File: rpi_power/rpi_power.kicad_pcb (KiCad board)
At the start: 2 copper layers, 99 x 99 mm, 131 parts, among them J1 POWER, J10 POWER, J2 Raspberry_Pi_2_3, J3 SENSORS, J4 ADCs, J5 DB25_Female, J6 SWITCHES, J7 PROG, J8 DB15_Female_MountingHoles, J9 GPIO, Q1 IRLML6344TRPBF, Q10 IRLML6344TRPBF, Q11 IRLML6344TRPBF, Q2 IRLML6344TRPBF, Q3 IRLML6344TRPBF, Q4 IRLML6344TRPBF, Q5 IRLML6344TRPBF, Q6 IRLML6344TRPBF, Q7 NPN, Q8 IRLML6344TRPBF, Q9 IRLML6344TRPBF, U1 TPS54625, U2 ATxmega16A4U-AU, U3 LM2936-3.3, Y1 Crystal

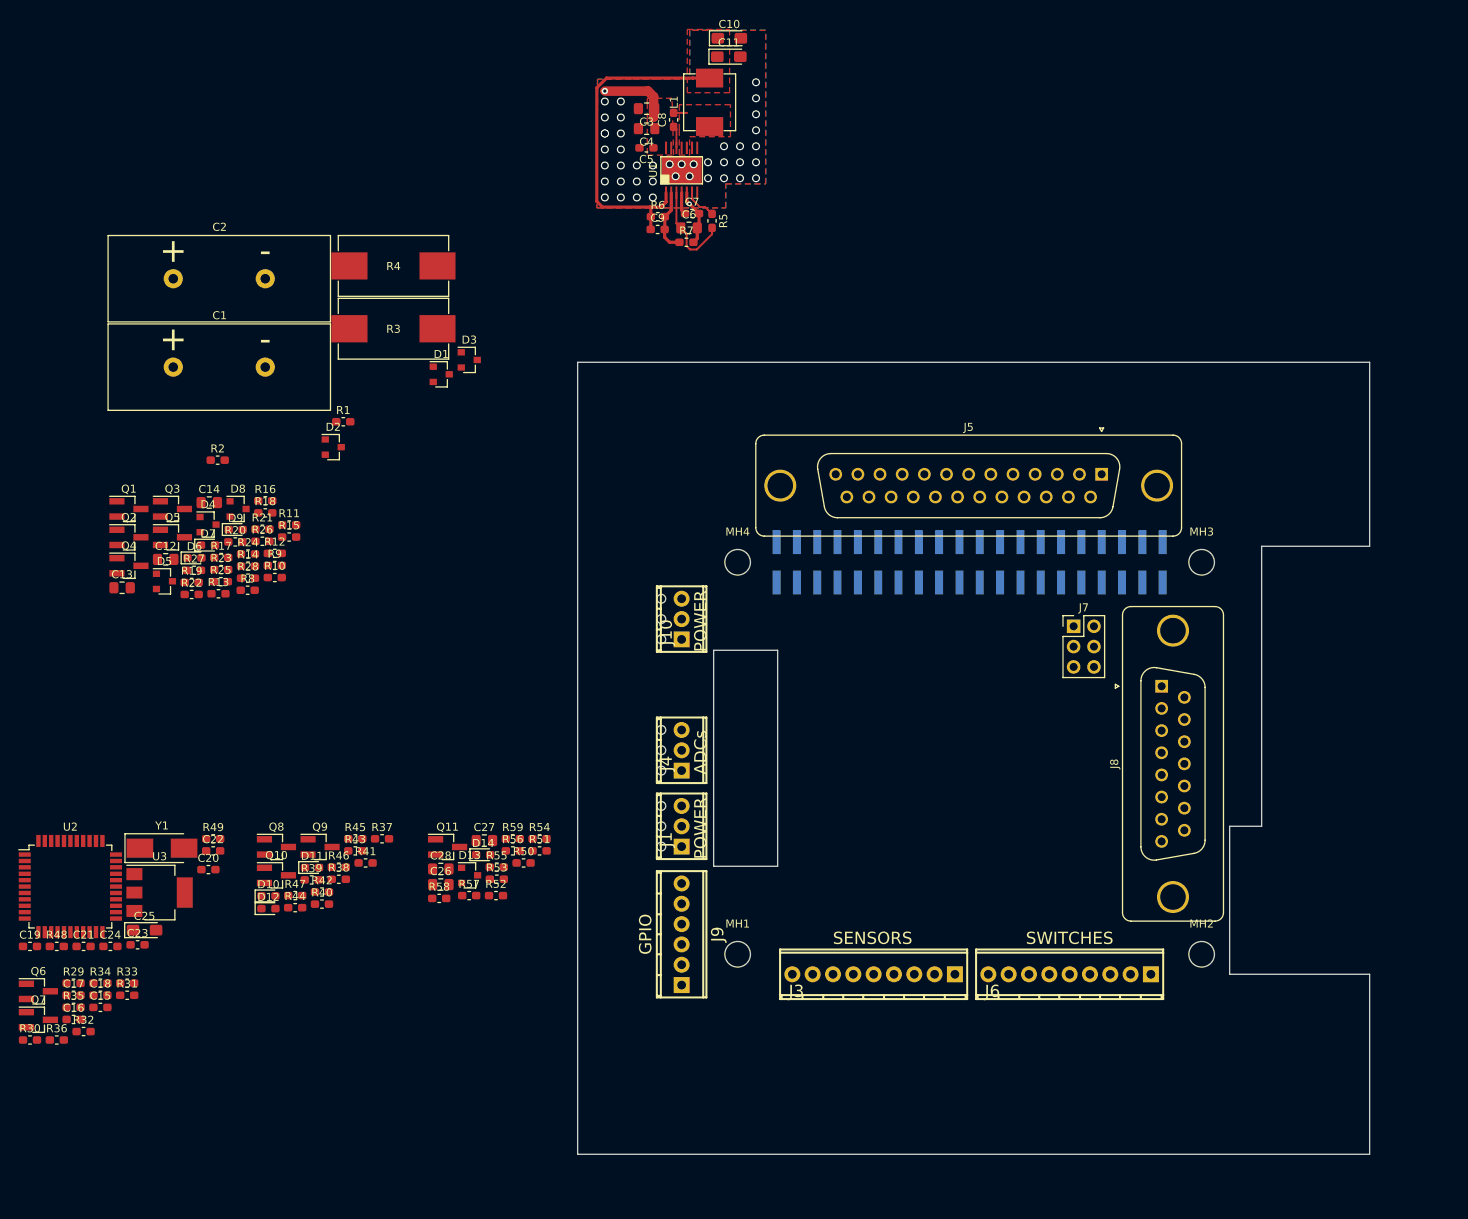
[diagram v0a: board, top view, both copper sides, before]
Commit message: Branched from cellar_board repo. Cleaned up unnecessary items.
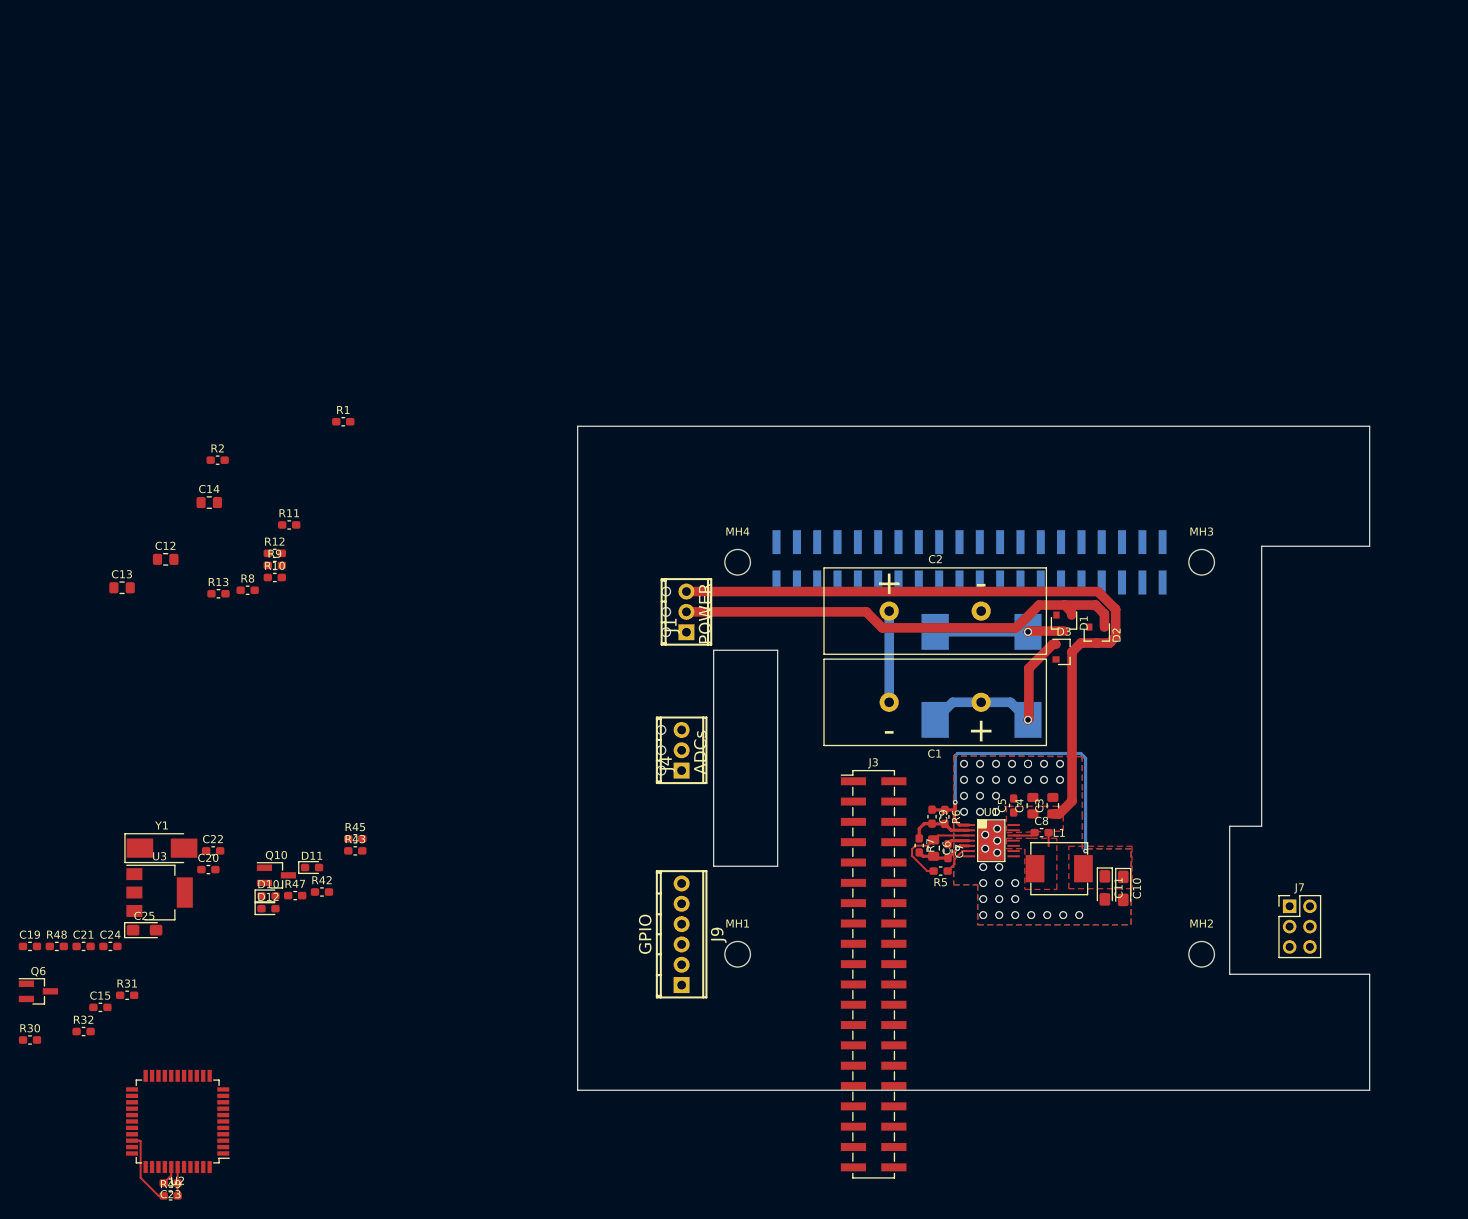
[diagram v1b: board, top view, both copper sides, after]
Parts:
- removed C16, C17, C18: 0.1uF/50V, Capacitor_SMD:C_0603_1608Metric_Pad1.05x0.95mm_HandSolder
- removed C26, C27, C28: UNKN, Capacitor_SMD:C_0805_2012Metric_Pad1.15x1.40mm_HandSolder
- removed D13, D4, D5, D8: SBR160S23-7, Diode_SMD:D_SOT-23_ANK
- removed D14, D6, D7, D9: LED_GREEN, LED_SMD:LED_0603_1608Metric_Pad1.05x0.95mm_HandSolder
- removed J10: POWER, w_conn_mpt:mpt_0,5-3-2,54
- removed J5: DB25_Female, Connectors_custom:DSUB-25_Female_Vertical_P2.77x2.84mm_MountingHoles
- removed J6: SWITCHES, w_conn_mpt:mpt_0,5-9-2,54
- removed J8: DB15_Female_MountingHoles, Connectors_custom:DSUB-15_Female_Vertical_P2.77x2.84mm_MountingHoles
- removed Q1, Q11, Q2, Q3, Q4, Q5, Q8, Q9: IRLML6344TRPBF, Package_TO_SOT_SMD:SOT-23_Handsoldering
- removed Q7: NPN, Package_TO_SOT_SMD:SOT-23_Handsoldering
- removed R14, R16, R17, R23, R26, R35, R37, R38, R41, R52: 10k, Resistor_SMD:R_0603_1608Metric_Pad1.05x0.95mm_HandSolder
- removed R15, R24, R25, R50, R51: 0, Resistor_SMD:R_0603_1608Metric_Pad1.05x0.95mm_HandSolder
- removed R18, R19, R27, R44, R46: 255, Resistor_SMD:R_0603_1608Metric_Pad1.05x0.95mm_HandSolder
- removed R20, R21, R28, R53: 1k, Resistor_SMD:R_0603_1608Metric_Pad1.05x0.95mm_HandSolder
- removed R22, R29, R33: 4.7k, Resistor_SMD:R_0603_1608Metric_Pad1.05x0.95mm_HandSolder
- removed R34, R40: 51k, Resistor_SMD:R_0603_1608Metric_Pad1.05x0.95mm_HandSolder
- removed R36, R39: 100k, Resistor_SMD:R_0603_1608Metric_Pad1.05x0.95mm_HandSolder
- removed R54, R55, R56, R57, R58, R59: UNKN, Resistor_SMD:R_0603_1608Metric_Pad1.05x0.95mm_HandSolder
- C12, C13, C14: value 10uF/25V -> UNKN
- J3: value SENSORS -> Raspberry_Pi_2_3; footprint w_conn_mpt:mpt_0,5-9-2,54 -> Connector_PinHeader_2.54mm:PinHeader_2x20_P2.54mm_Vertical_SMD
- R10: value 10k -> UNKN
- R11, R12, R13: value 0 -> UNKN
- R3, R4: moved to B.Cu
- R8, R9: value 4.7k -> UNKN
- moved C10 117.1 mm to (168.2, 111.8), turned to 270 degrees
- moved C11 114.0 mm to (165.9, 111.7), turned to 270 degrees
- moved L1 105.3 mm to (160.2, 109.3), turned to 0 degrees
- moved C3 100.8 mm to (159.4, 101.4), turned to 90 degrees
- moved C8 100.3 mm to (158.0, 104.8), turned to 0 degrees
- moved C1 98.8 mm to (144.7, 88.5), turned to 180 degrees
- moved C2 98.7 mm to (144.7, 77.1)
- moved D2 98.3 mm to (164.9, 80.1), turned to 270 degrees
- moved C4 97.4 mm to (156.9, 101.4), turned to 90 degrees
- moved C5 94.1 mm to (154.5, 101.4), turned to 90 degrees
- moved U1 92.3 mm to (151.7, 105.8), turned to 0 degrees
- moved R3 90.4 mm to (156.3, 85.2), turned to 90 degrees
- moved R5 86.2 mm to (145.4, 109.6), turned to 180 degrees
- moved C7 85.9 mm to (146.3, 107.1), turned to 270 degrees
- moved R4 84.9 mm to (144.7, 85.2), turned to 90 degrees
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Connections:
- C12 pad 1: HEAT_LEVER_F -> ADC1
- C13 pad 1: FAN_LEVER_F -> ADC2
- C14 pad 1: DEHUM_LEVER_F -> ADC3
- J2 pad 10: UART_RX_3V3 -> 10
- J2 pad 11: DHT22_EXT -> 11
- J2 pad 12: SERVO_PWM -> 12
- J2 pad 13: SERVO_ON-OFF -> 13
- J2 pad 16: FAN_LEVER_F -> 16
- J2 pad 18: LIGHT_SENSOR -> 18
- J2 pad 19: SPI0_MOSI -> 19
- J2 pad 21: SPI0_MISO -> 21
- J2 pad 22: HEAT_SWITCH -> 22
- J2 pad 23: SPI0_SCLK -> 23
- J2 pad 24: SPI0_CE -> 24
- J2 pad 26: SPI1_CE -> 26
- J2 pad 27: RESET_LEVER -> 27
- J2 pad 28: SWITCH0 -> 28
- J2 pad 29: HEAT_LEVER_F -> 29
- J2 pad 31: DEHUM_SWITCH -> 31
- J2 pad 32: DEHUM_LEVER_F -> 32
- J2 pad 33: FAN_SWITCH -> 33
- J2 pad 35: SPI1_MISO -> 35
- J2 pad 38: SPI1_MOSI -> 38
- J2 pad 40: SPI1_SCLK -> 40
- J2 pad 7: DHT22_INT -> 7
- J2 pad 8: UART_TX_3V3 -> 8
- J3 pad 1: GND -> +3V3
- J3 pad 2: +3V3 -> +5V
- J3 pad 3: DHT22_INT -> I2C_SDA
- J3 pad 4: GND -> +5V
- J3 pad 5: +3V3 -> I2C_SCL
- J3 pad 6: DHT22_EXT -> GND
- J3 pad 7: +3V3 -> 7
- J3 pad 8: LIGHTSEN_SIG -> 8
- J7 pad 3: Net-(J7-Pad3) -> (no net)
- J7 pad 4: Net-(J7-Pad4) -> (no net)
- R10 pad 1: GND -> ADC2
- R10 pad 2: HEAT_LEVER_F -> ADC2
- R11 pad 1: HEAT_SWITCH+ -> ADC2
- R11 pad 2: +12V -> GND
- R12 pad 1: +5V -> ADC3
- R12 pad 2: HEAT_SWITCH+ -> ADC3
- R13 pad 1: FAN_SWITCH+ -> ADC3
- R13 pad 2: +12V -> GND
- R43 pad 1: Net-(D10-Pad1) -> Net-(Q10-Pad3)
- R43 pad 2: Net-(Q10-Pad3) -> Net-(D10-Pad1)
- R45 pad 1: Net-(D11-Pad1) -> GND
- R45 pad 2: GND -> Net-(D11-Pad1)
- R8 pad 1: HEAT_LEVER_F -> ADC1
- R8 pad 2: HEAT_LEVER_IN -> ADC1
- R9 pad 1: FAN_LEVER_F -> ADC1
- R9 pad 2: FAN_LEVER_IN -> GND
- U2 pad 1: Net-(U2-Pad1) -> (no net)
- U2 pad 12: Net-(U2-Pad12) -> (no net)
- U2 pad 13: Net-(U2-Pad13) -> (no net)
- U2 pad 14: Net-(U2-Pad14) -> (no net)
- U2 pad 15: Net-(U2-Pad15) -> (no net)
- U2 pad 16: Net-(U2-Pad16) -> (no net)
- U2 pad 17: Net-(U2-Pad17) -> (no net)
- U2 pad 2: Net-(U2-Pad2) -> (no net)
- U2 pad 25: Net-(U2-Pad25) -> (no net)
- U2 pad 26: Net-(U2-Pad26) -> (no net)
- U2 pad 27: Net-(U2-Pad27) -> (no net)
- U2 pad 3: Net-(U2-Pad3) -> (no net)
- U2 pad 4: Net-(U2-Pad4) -> (no net)
- U2 pad 44: Net-(U2-Pad44) -> (no net)
- U2 pad 5: Net-(U2-Pad5) -> (no net)
- U2 pad 6: Net-(U2-Pad6) -> (no net)
- U2 pad 7: Net-(U2-Pad7) -> (no net)
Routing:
- net VCOND: track 8.99 -> 86.0 mm, vias 1 -> 0
- net +12V: track 0.00 -> 58.0 mm
- net Net-(C1-Pad1): track 0.00 -> 24.6 mm, vias 0 -> 1
- net Net-(D1-Pad1): track 0.00 -> 16.1 mm, vias 0 -> 1
- net Net-(C1-Pad2): track 0.00 -> 11.4 mm
- net VCC: track 0.00 -> 9.49 mm
- net Net-(C23-Pad1): track 0.00 -> 3.60 mm
- net GND: track 7.12 -> 9.52 mm
- net +5V: track 42.0 -> 41.2 mm, vias 0 -> 2
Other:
- board size 99 x 99 mm -> 99 x 83 mm

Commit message: Components placed.
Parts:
- C12, C13, C14, C15, Q10, Q6, R1, R10, R11, R12, R13, R2, R30, R31, R32, R42, R43, R45, R47, R8, R9, U3: moved to B.Cu
- moved R2 129.4 mm to (171.6, 114.3), turned to 270 degrees
- moved R48 119.2 mm to (154.0, 114.3), turned to 180 degrees
- moved C19 117.0 mm to (148.1, 109.5), turned to 90 degrees
- moved R1 116.4 mm to (169.9, 114.3), turned to 90 degrees
- moved R47 109.0 mm to (173.7, 114.3), turned to 90 degrees
- moved D12 108.5 mm to (169.9, 114.3), turned to 270 degrees
- moved R49 105.7 mm to (145.1, 106.0), turned to 270 degrees
- moved C13 105.2 mm to (139.7, 115.7)
- moved Q6 104.8 mm to (135.7, 105.9)
- moved C14 104.0 mm to (143.9, 115.7)
- moved R30 103.6 mm to (132.1, 105.9), turned to 90 degrees
- moved C23 103.5 mm to (143.5, 106.0), turned to 90 degrees
- moved Y1 103.0 mm to (151.0, 107.6), turned to 90 degrees
- moved C24 100.1 mm to (137.2, 89.5), turned to 270 degrees
- moved R32 99.8 mm to (135.9, 109.5), turned to 90 degrees
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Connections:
- J4 pad 1: ADC1 -> ADC3_IN
- J4 pad 2: ADC2 -> ADC2_IN
- J4 pad 3: ADC3 -> ADC1_IN
- J9 pad 2: GPIO0 -> GPIO4
- J9 pad 3: GPIO1 -> GPIO3
- J9 pad 5: GPIO3 -> GPIO1
- J9 pad 6: GPIO4 -> GPIO0
- R10 pad 1: ADC2 -> ADC2_IN
- R12 pad 1: ADC3 -> ADC3_IN
- R8 pad 1: ADC1 -> ADC1_IN
- U2 pad 20: GPIO0 -> (no net)
- U2 pad 21: GPIO1 -> (no net)
- U2 pad 22: GPIO2 -> (no net)
- U2 pad 23: GPIO3 -> GPIO0
- U2 pad 24: GPIO4 -> GPIO1
- U2 pad 25: (no net) -> GPIO2
- U2 pad 26: (no net) -> GPIO3
- U2 pad 27: (no net) -> GPIO4
- U2 pad 28: VCOND_MEASURE -> ADC0
- U2 pad 29: WATCHDOG -> ADC1
- U2 pad 32: POWER_STATE -> ADC2
- U2 pad 33: ENABLE -> ADC3
- U2 pad 4: (no net) -> VCOND_MEASURE
- U2 pad 40: ADC0 -> (no net)
- U2 pad 41: ADC1 -> (no net)
- U2 pad 42: ADC2 -> (no net)
- U2 pad 43: ADC3 -> (no net)
- U2 pad 5: (no net) -> WATCHDOG
- U2 pad 6: (no net) -> POWER_STATE
- U2 pad 7: (no net) -> ENABLE
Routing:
- net VCOND: track 86.0 -> 3.06 mm
- net +12V: track 58.0 -> 0.00 mm
- net Net-(C1-Pad1): track 24.6 -> 0.00 mm, vias 1 -> 0
- net Net-(D1-Pad1): track 16.1 -> 0.00 mm, vias 1 -> 0
- net Net-(C1-Pad2): track 11.4 -> 0.00 mm
- net VCC: track 9.49 -> 0.00 mm
- net Net-(C23-Pad1): track 3.60 -> 0.00 mm
- net GND: track 9.52 -> 7.12 mm, vias 42 -> 50
- net WATCHDOG: vias 0 -> 1
- net POWER_STATE: vias 0 -> 1
- net LED_RUN: vias 0 -> 1
- net I2C_SDA: vias 0 -> 1
- net I2C_SCL: vias 0 -> 1
- net 8: vias 0 -> 3
- net 7: vias 0 -> 1
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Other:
- board size 99 x 83 mm -> 69 x 57.4 mm

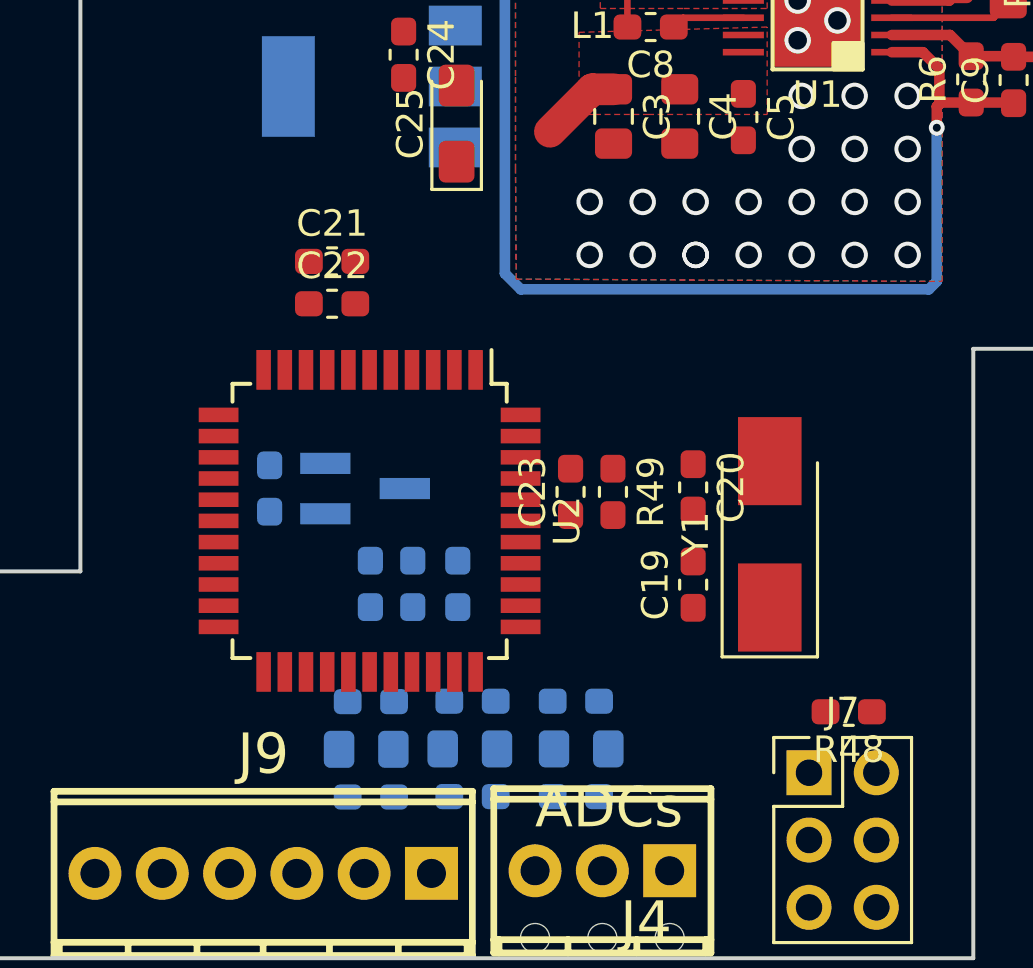
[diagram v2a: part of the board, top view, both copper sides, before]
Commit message: Small changes to components positions.
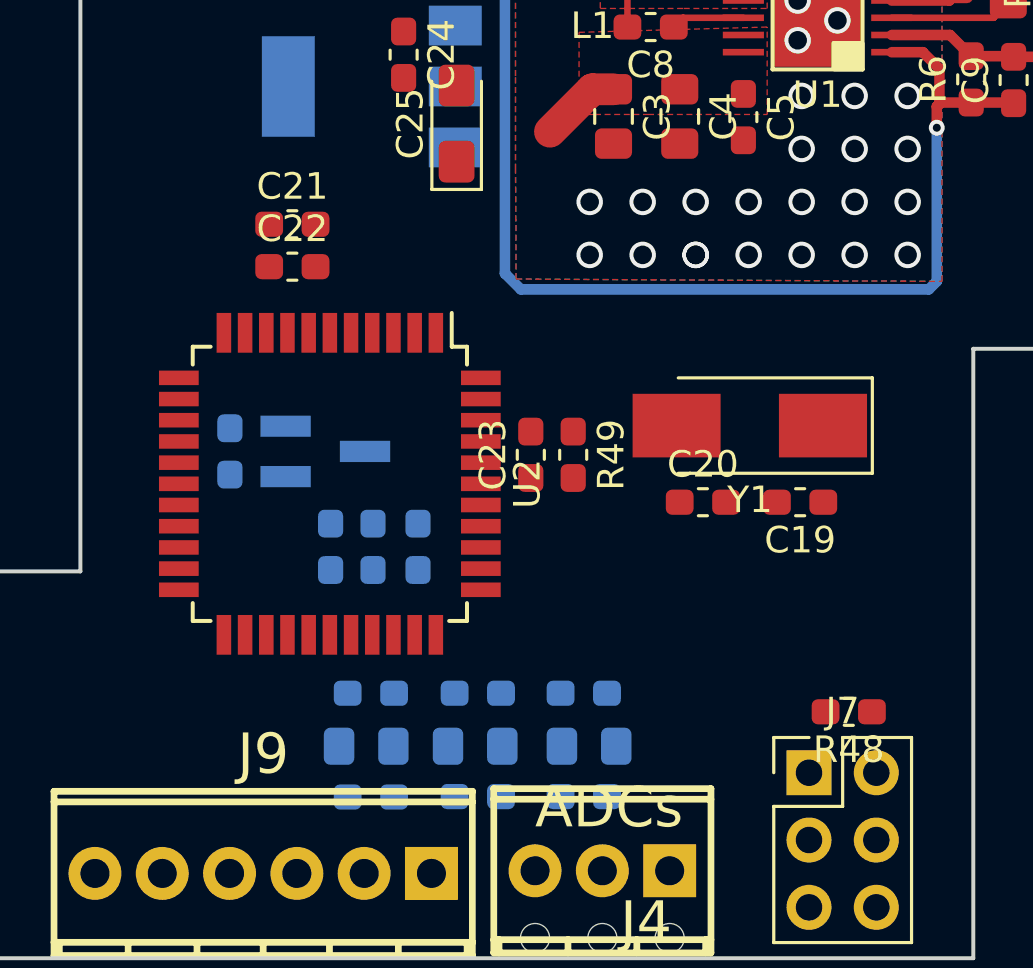
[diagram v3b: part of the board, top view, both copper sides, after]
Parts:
- moved C19 5.10 mm to (152.2, 106.4), turned to 180 degrees
- moved Y1 4.17 mm to (150.3, 103.5), turned to 180 degrees
- moved C22 2.05 mm to (133.0, 97.5)
- moved C23 2.05 mm to (142.0, 104.6)
- moved Q6 2.05 mm to (134.2, 104.5)
- moved R30 2.05 mm to (130.6, 104.5)
- moved R49 2.05 mm to (143.6, 104.6)
- moved U2 2.05 mm to (134.4, 105.7)
- moved C15 2.05 mm to (136.0, 108.1)
- moved C21 2.05 mm to (133.0, 95.9)
- moved R31 2.05 mm to (137.7, 108.1)
- moved R32 2.05 mm to (134.4, 108.1)
- moved C20 0.67 mm to (148.5, 106.4), turned to 0 degrees
- moved R13 0.42 mm to (144.0, 113.6)
- moved R10 0.36 mm to (140.0, 113.6)
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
